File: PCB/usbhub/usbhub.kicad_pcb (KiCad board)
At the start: 2 copper layers, 30.8 x 54.8 mm, 35 parts, among them U1 SL2.1S, U2 SL2.1S

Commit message: case and assembly
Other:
- board size 30.8 x 54.8 mm -> 30.7 x 55 mm
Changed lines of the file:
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@@
 	)
 	(gr_rect
-		(start 148.5 41.75)
+		(start 148.524591 41.518764)
 		(end 179.25 96.5)
+		(radius 2)
 		(stroke
 			(width 0.05)
-			(type default)
+			(type solid)
 		)
 		(fill no)

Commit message: Update usbhub.kicad_pcb
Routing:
- net GND: vias 13 -> 14
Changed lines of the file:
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@@
+	)
+	(via
+		(at 168.22 85.05)
+		(size 0.6)
+		(drill 0.3)
+		(layers "F.Cu" "B.Cu")
+		(net "GND")
 	)
 	(via

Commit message: Update usbhub.kicad_pcb
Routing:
- net /D1B-: track 36.3 -> 36.8 mm
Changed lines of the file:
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@@
+	)
+	(segment
+		(start 170.775 78.594123)
+		(end 170.775 76.075389)
+		(width 0.2)
+		(layer "F.Cu")
+		(net "/D1B-")
+	)
+	(segment
+		(start 169.475 89.55)
+		(end 170.775 88.25)
+		(width 0.2)
+		(layer "F.Cu")
+		(net "/D1B-")
+	)
+	(segment
+		(start 170.324901 84.329337)
+		(end 170.535 84.329337)
+		(width 0.2)
+		(layer "F.Cu")
+		(net "/D1B-")
+	)
+	(segment
+		(start 170.535 81.329337)
+		(end 170.124889 81.329337)
+		(width 0.2)
+		(layer "F.Cu")
+		(net "/D1B-")
+	)
+	(segment
+		(start 170.775 72.593198)
+		(end 169.541782 71.35998)
+		(width 0.2)
+		(layer "F.Cu")
+		(net "/D1B-")
+	)
+	(segment
+		(start 170.775 80.489337)
+		(end 170.775 79.794123)
+		(width 0.2)
+		(layer "F.Cu")
+		(net "/D1B-")
+	)
+	(segment
+		(start 170.324901 86.729337)
+		(end 170.535 86.729337)
+		(width 0.2)
+		(layer "F.Cu")
+		(net "/D1B-")
+	)
+	(segment
+		(start 170.535 84.929337)
+		(end 170.324901 84.929337)
+		(width 0.2)
+		(layer "F.Cu")
+		(net "/D1B-")
+	)
+	(segment
+		(start 169.884889 81.089337)
+		(end 169.884889 80.969337)
+		(width 0.2)
+		(layer "F.Cu")
+		(net "/D1B-")
+	)
+	(segment
+		(start 169.884913 83.489337)
+		(end 169.884913 83.369337)
+		(width 0.2)
+		(layer "F.Cu")
+		(net "/D1B-")
+	)
+	(segment
+		(start 170.124889 80.729337)
+		(end 170.535 80.729337)
+		(width 0.2)
+		(layer "F.Cu")
+		(net "/D1B-")
+	)
+	(segment
+		(start 169.884913 82.289337)
+		(end 169.884913 82.169337)
+		(width 0.2)
+		(layer "F.Cu")
+		(net "/D1B-")
+	)
+	(segment
+		(start 170.324901 85.529337)
+		(end 170.535 85.529337)
+		(width 0.2)
+		(layer "F.Cu")
+		(net "/D1B-")
+	)
+	(segment
+		(start 170.535 86.129337)
+		(end 170.324901 86.129337)
+		(width 0.2)
+		(layer "F.Cu")
+		(net "/D1B-")
 	)
 	(segment
@@
 	)
 	(segment
-		(start 169.475 89.55)
-		(end 170.775 88.25)
-		(width 0.2)
-		(layer "F.Cu")
-		(net "/D1B-")
-	)
-	(segment
-		(start 170.324901 84.329337)
-		(end 170.535 84.329337)
-		(width 0.2)
-		(layer "F.Cu")
-		(net "/D1B-")
-	)
-	(segment
-		(start 170.535 81.329337)
-		(end 170.124889 81.329337)
-		(width 0.2)
-		(layer "F.Cu")
-		(net "/D1B-")
-	)
-	(segment
-		(start 170.324901 86.729337)
-		(end 170.535 86.729337)
-		(width 0.2)
-		(layer "F.Cu")
-		(net "/D1B-")
-	)
-	(segment
-		(start 170.535 84.929337)
-		(end 170.324901 84.929337)
-		(width 0.2)
-		(layer "F.Cu")
-		(net "/D1B-")
-	)
-	(segment
-		(start 169.884889 81.089337)
-		(end 169.884889 80.969337)
-		(width 0.2)
-		(layer "F.Cu")
-		(net "/D1B-")
-	)
-	(segment
-		(start 169.884913 83.489337)
-		(end 169.884913 83.369337)
-		(width 0.2)
-		(layer "F.Cu")
-		(net "/D1B-")
-	)
-	(segment
-		(start 170.775 72.593198)
-		(end 169.541782 71.35998)
-		(width 0.2)
-		(layer "F.Cu")
-		(net "/D1B-")
-	)
-	(segment
-		(start 170.124889 80.729337)
-		(end 170.535 80.729337)
-		(width 0.2)
-		(layer "F.Cu")
-		(net "/D1B-")
-	)
-	(segment
-		(start 169.884913 82.289337)
-		(end 169.884913 82.169337)
-		(width 0.2)
-		(layer "F.Cu")
-		(net "/D1B-")
-	)
-	(segment
-		(start 170.324901 85.529337)
-		(end 170.535 85.529337)
-		(width 0.2)
-		(layer "F.Cu")
-		(net "/D1B-")
-	)
-	(segment
-		(start 170.535 86.129337)
-		(end 170.324901 86.129337)
+		(start 170.084901 84.689337)
+		(end 170.084901 84.569337)
+		(width 0.2)
+		(layer "F.Cu")
+		(net "/D1B-")
+	)
+	(segment
+		(start 170.775 81.689337)
+		(end 170.775 81.569337)
+		(width 0.2)
+		(layer "F.Cu")
+		(net "/D1B-")
+	)
+	(segment
+		(start 161.39002 68.842073)
+		(end 161.39002 67.89002)
+		(width 0.2)
+		(layer "F.Cu")
+		(net "/D1B-")
+	)
+	(segment
+		(start 170.124913 81.929337)
+		(end 170.535 81.929337)
+		(width 0.2)
+		(layer "F.Cu")
+		(net "/D1B-")
+	)
+	(segment
+		(start 170.775 88.25)
+		(end 170.775 87.569337)
+		(width 0.2)
+		(layer "F.Cu")
+		(net "/D1B-")
+	)
+	(segment
+		(start 170.535 82.529337)
+		(end 170.124913 82.529337)
+		(width 0.2)
+		(layer "F.Cu")
+		(net "/D1B-")
+	)
+	(segment
+		(start 170.084901 87.089337)
+		(end 170.084901 86.969337)
+		(width 0.2)
+		(layer "F.Cu")
+		(net "/D1B-")
+	)
+	(segment
+		(start 170.535 83.729337)
+		(end 170.124913 83.729337)
+		(width 0.2)
+		(layer "F.Cu")
+		(net "/D1B-")
+	)
+	(segment
+		(start 170.775 82.889337)
+		(end 170.775 82.769337)
+		(width 0.2)
+		(layer "F.Cu")
+		(net "/D1B-")
+	)
+	(segment
+		(start 170.775 78.721951)
+		(end 170.775 78.594123)
+		(width 0.2)
+		(layer "F.Cu")
+		(net "/D1B-")
+	)
+	(segment
+		(start 170.302828 79.321951)
+		(end 170.302828 79.194123)
+		(width 0.2)
+		(layer "F.Cu")
+		(net "/D1B-")
+	)
+	(segment
+		(start 170.775 85.289337)
+		(end 170.775 85.169337)
+		(width 0.2)
+		(layer "F.Cu")
+		(net "/D1B-")
+	)
+	(segment
+		(start 170.535 87.329337)
+		(end 170.324901 87.329337)
 		(width 0.2)
 		(layer "F.Cu")
@@
 	)
 	(segment
+		(start 170.775 76.075389)
+		(end 170.775 72.593198)
+		(width 0.2)
+		(layer "F.Cu")
+		(net "/D1B-")
+	)
+	(segment
 		(start 169.541782 71.35998)
 		(end 163.907927 71.35998)
-		(width 0.2)
-		(layer "F.Cu")
-		(net "/D1B-")
-	)
-	(segment
-		(start 170.084901 84.689337)
-		(end 170.084901 84.569337)
-		(width 0.2)
-		(layer "F.Cu")
-		(net "/D1B-")
-	)
-	(segment
-		(start 170.775 81.689337)
-		(end 170.775 81.569337)
-		(width 0.2)
-		(layer "F.Cu")
-		(net "/D1B-")
-	)
-	(segment
-		(start 170.124913 81.929337)
-		(end 170.535 81.929337)
-		(width 0.2)
-		(layer "F.Cu")
-		(net "/D1B-")
-	)
-	(segment
-		(start 170.775 88.25)
-		(end 170.775 87.569337)
-		(width 0.2)
-		(layer "F.Cu")
-		(net "/D1B-")
-	)
-	(segment
-		(start 170.535 82.529337)
-		(end 170.124913 82.529337)
-		(width 0.2)
-		(layer "F.Cu")
-		(net "/D1B-")
-	)
-	(segment
-		(start 170.084901 87.089337)
-		(end 170.084901 86.969337)
-		(width 0.2)
-		(layer "F.Cu")
-		(net "/D1B-")
-	)
-	(segment
-		(start 170.535 83.729337)
-		(end 170.124913 83.729337)
-		(width 0.2)
-		(layer "F.Cu")
-		(net "/D1B-")
-	)
-	(segment
-		(start 170.775 82.889337)
-		(end 170.775 82.769337)
-		(width 0.2)
-		(layer "F.Cu")
-		(net "/D1B-")
-	)
-	(segment
-		(start 161.39002 68.842073)
-		(end 161.39002 67.89002)
-		(width 0.2)
-		(layer "F.Cu")
-		(net "/D1B-")
-	)
-	(segment
-		(start 170.775 80.489337)
-		(end 170.775 72.593198)
-		(width 0.2)
-		(layer "F.Cu")
-		(net "/D1B-")
-	)
-	(segment
-		(start 170.775 85.289337)
-		(end 170.775 85.169337)
-		(width 0.2)
-		(layer "F.Cu")
-		(net "/D1B-")
-	)
-	(segment
-		(start 170.535 87.329337)
-		(end 170.324901 87.329337)
 		(width 0.2)
 		(layer "F.Cu")
@@
 	)
 	(arc
+		(start 170.302828 79.194123)
+		(mid 170.371976 79.027185)
+		(end 170.538914 78.958037)
+		(width 0.2)
+		(layer "F.Cu")
+		(net "/D1B-")
+	)
+	(arc
 		(start 170.775 82.769337)
 		(mid 170.704706 82.599631)
@@
 	)
 	(arc
+		(start 170.538914 78.958037)
+		(mid 170.705852 78.888889)
+		(end 170.775 78.721951)
+		(width 0.2)
+		(layer "F.Cu")
+		(net "/D1B-")
+	)
+	(arc
 		(start 169.884913 83.369337)
 		(mid 169.955207 83.199631)
@@
 	)
 	(arc
+		(start 170.775 79.794123)
+		(mid 170.705852 79.627185)
+		(end 170.538914 79.558037)
+		(width 0.2)
+		(layer "F.Cu")
+		(net "/D1B-")
+	)
+	(arc
 		(start 170.124889 81.329337)
 		(mid 169.955183 81.259043)
@@
 		(mid 170.704706 81.399631)
 		(end 170.535 81.329337)
+		(width 0.2)
+		(layer "F.Cu")
+		(net "/D1B-")
+	)
+	(arc
+		(start 170.538914 79.558037)
+		(mid 170.371976 79.488889)
+		(end 170.302828 79.321951)
 		(width 0.2)
 		(layer "F.Cu")
@@
 	)
 	(generated
+		(type tuning_pattern)
+		(name "Tuning Pattern")
+		(layer "F.Cu")
+		(base_line
+			(pts
+				(xy 170.775 79.794123) (xy 170.775 76.075389)
+			)
+		)
+		(base_line_coupled
+			(pts
+				(xy 171.225 79.794123) (xy 171.225 79.810099)
+			)
+		)
+		(corner_radius_percent 80)
+		(end
+			(xy 170.775 76.075389)
+		)
+		(initial_side "left")
+		(is_time_domain no)
+		(last_diff_pair_gap 0.18)
+		(last_netname "/D1B-")
+		(last_status "tuned")
+		(last_track_width 0.2)
+		(last_tuning_length -5.6e-05)
+		(max_amplitude 1)
+		(min_amplitude 0.2)
+		(min_spacing 0.6)
+		(origin
+			(xy 170.775 79.794123)
+		)
+		(override_custom_rules no)
+		(rounded yes)
+		(single_sided no)
+		(target_delay 1000000)
+		(target_delay_max 1000000)
+		(target_delay_min 0)
+		(target_length 1000000)
+		(target_length_max 1000000)
+		(target_length_min 0)
+		(target_skew 0)
+		(target_skew_max 0.1)
+		(target_skew_min -0.1)
+		(tuning_mode "diff_pair_skew")
+		(members "1dece349-dbe6-4893-8c04-211b6d402d7a" "26bfc59c-0bca-4a53-af13-9448fa790285"
+			"31407be5-377e-49e6-b739-af8d52b4daab" "53a43092-9930-406d-b0c2-06b6def7a89c"
+			"75226c4a-ea9a-4ce0-b9c3-285e020652f5" "aa32028f-71d7-4b5e-87e4-8afc0a5836df"
+			"aab755b0-ae1c-4e58-aaa0-9a94909e4790"
+		)
+	)
+	(generated

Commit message: update all the steps
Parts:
- added H1: MountingHole, MountingHole:MountingHole_3.2mm_M3, F.Cu at (152.5, 45.5)
- added H2: MountingHole, MountingHole:MountingHole_3.2mm_M3, F.Cu at (163.5, 93.0)
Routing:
- net /VBUS: track 187.3 -> 185.5 mm
- net /D4B-: track 21.0 -> 22.6 mm
- net /D4B+: track 22.5 -> 23.8 mm

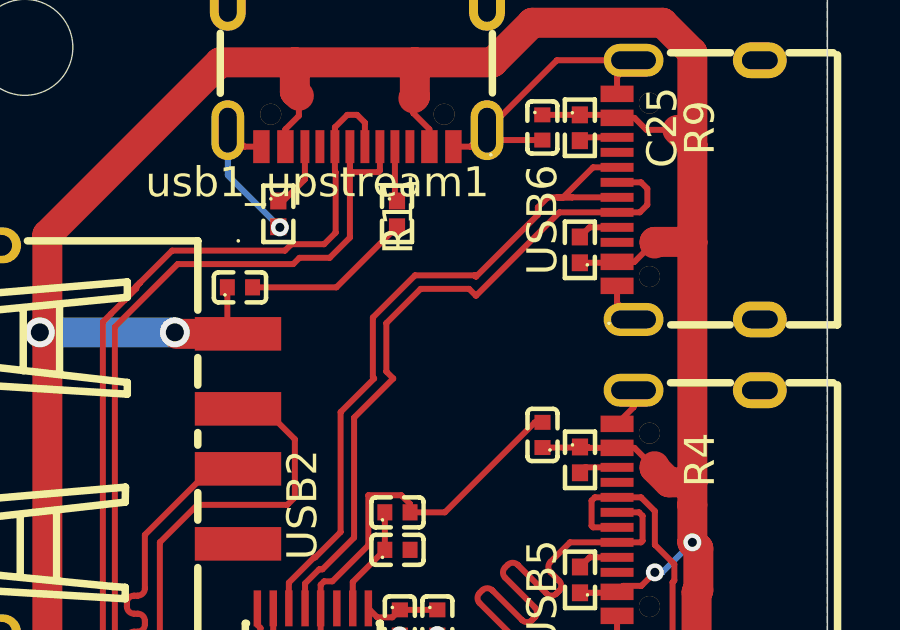
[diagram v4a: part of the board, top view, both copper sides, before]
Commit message: no curvy trace around nonexistent hole
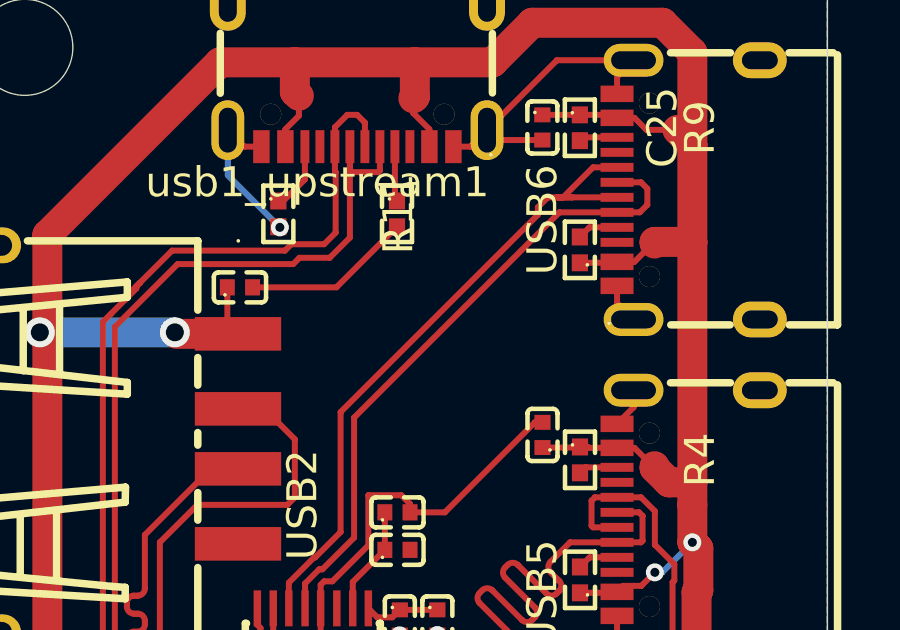
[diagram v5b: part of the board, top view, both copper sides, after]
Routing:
- net /D4B-: track 22.6 -> 21.0 mm
- net /D4B+: track 23.8 -> 22.5 mm
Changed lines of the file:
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@@
 	)
 	(segment
-		(start 171.44 49.5)
-		(end 170.44 50.5)
+		(start 169.934314 50.5)
+		(end 170.75 50.5)
 		(width 0.2)
 		(layer "F.Cu")
@@
 	)
 	(segment
+		(start 171.44 49.5)
+		(end 170.44 50.5)
+		(width 0.2)
+		(layer "F.Cu")
+		(net "/D4B+")
+	)
+	(segment
 		(start 172.24 50.5)
 		(end 170.75 50.5)
+		(width 0.2)
+		(layer "F.Cu")
+		(net "/D4B+")
+	)
+	(segment
+		(start 161.3 63.34363)
+		(end 162.14363 62.5)
+		(width 0.2)
+		(layer "F.Cu")
+		(net "/D4B+")
+	)
+	(segment
+		(start 170.44 50.5)
+		(end 170.25 50.5)
+		(width 0.2)
+		(layer "F.Cu")
+		(net "/D4B+")
+	)
+	(segment
+		(start 163.025 57.656802)
+		(end 169.6 51.081802)
+		(width 0.2)
+		(layer "F.Cu")
+		(net "/D4B+")
+	)
+	(segment
+		(start 169.6 51.081802)
+		(end 169.6 50.834314)
+		(width 0.2)
+		(layer "F.Cu")
+		(net "/D4B+")
+	)
+	(segment
+		(start 162.181802 62.5)
+		(end 163.025 61.656802)
+		(width 0.2)
+		(layer "F.Cu")
+		(net "/D4B+")
+	)
+	(segment
+		(start 172.24 49.5)
+		(end 171.44 49.5)
+		(width 0.2)
+		(layer "F.Cu")
+		(net "/D4B+")
+	)
+	(segment
+		(start 170.25 50.5)
+		(end 170.75 50.5)
+		(width 0.2)
+		(layer "F.Cu")
+		(net "/D4B+")
+	)
+	(segment
+		(start 163.025 61.656802)
+		(end 163.025 57.656802)
+		(width 0.2)
+		(layer "F.Cu")
+		(net "/D4B+")
+	)
+	(segment
+		(start 169.6 50.834314)
+		(end 169.934314 50.5)
 		(width 0.2)
 		(layer "F.Cu")
@@
 	)
 	(segment
-		(start 169.934314 50.5)
-		(end 170.75 50.5)
+		(start 161.84 63.725)
+		(end 161.84 63.369315)
 		(width 0.2)
 		(layer "F.Cu")
-		(net "/D4B+")
+		(net "/D4B-")
 	)
 	(segment
-		(start 162.181802 62.5)
-		(end 163.025 61.656802)
-		(width 0.2)
-		(layer "F.Cu")
-		(net "/D4B+")
-	)
-	(segment
-		(start 170.44 50.5)
-		(end 170.25 50.5)
-		(width 0.2)
-		(layer "F.Cu")
-		(net "/D4B+")
-	)
-	(segment
-		(start 164.10002 54.505896)
-		(end 165.505896 53.10002)
-		(width 0.2)
-		(layer "F.Cu")
-		(net "/D4B+")
-	)
-	(segment
-		(start 164.10002 56.494104)
-		(end 164.10002 54.505896)
-		(width 0.2)
-		(layer "F.Cu")
-		(net "/D4B+")
-	)
-	(segment
-		(start 167.494104 53.10002)
-		(end 167.537943 53.143859)
-		(width 0.2)
-		(layer "F.Cu")
-		(net "/D4B+")
-	)
-	(segment
-		(start 172.24 49.5)
-		(end 171.44 49.5)
-		(width 0.2)
-		(layer "F.Cu")
-		(net "/D4B+")
-	)
-	(segment
-		(start 167.537943 53.143859)
-		(end 169.6 51.081802)
-		(width 0.2)
-		(layer "F.Cu")
-		(net "/D4B+")
-	)
-	(segment
-		(start 170.25 50.5)
-		(end 170.75 50.5)
-		(width 0.2)
-		(layer "F.Cu")
-		(net "/D4B+")
-	)
-	(segment
-		(start 164.143859 56.537943)
-		(end 164.10002 56.494104)
-		(width 0.2)
-		(layer "F.Cu")
-		(net "/D4B+")
-	)
-	(segment
-		(start 169.6 50.834314)
-		(end 169.934314 50.5)
-		(width 0.2)
-		(layer "F.Cu")
-		(net "/D4B+")
-	)
-	(segment
-		(start 161.3 63.34363)
-		(end 162.14363 62.5)
-		(width 0.2)
-		(layer "F.Cu")
-		(net "/D4B+")
-	)
-	(segment
-		(start 163.025 57.656802)
-		(end 164.143859 56.537943)
-		(width 0.2)
-		(layer "F.Cu")
-		(net "/D4B+")
-	)
-	(segment
-		(start 163.025 61.656802)
-		(end 163.025 57.656802)
-		(width 0.2)
-		(layer "F.Cu")
-		(net "/D4B+")
-	)
-	(segment
-		(start 165.505896 53.10002)
-		(end 167.494104 53.10002)
-		(width 0.2)
-		(layer "F.Cu")
-		(net "/D4B+")
-	)
-	(segment
-		(start 169.6 51.081802)
-		(end 169.6 50.834314)
-		(width 0.2)
-		(layer "F.Cu")
-		(net "/D4B+")
-	)
-	(segment
-		(start 164.780241 56.537957)
-		(end 164.55 56.307716)
+		(start 163.475 57.843198)
+		(end 170.318198 51)
 		(width 0.2)
 		(layer "F.Cu")
@@
 	)
 	(segment
-		(start 162.309315 62.9)
-		(end 162.418198 62.9)
-		(width 0.2)
-		(layer "F.Cu")
-		(net "/D4B-")
-	)
-	(segment
 		(start 173 51)
 		(end 172.24 51)
-		(width 0.2)
-		(layer "F.Cu")
-		(net "/D4B-")
-	)
-	(segment
-		(start 164.55 54.692284)
-		(end 165.692284 53.55)
 		(width 0.2)
 		(layer "F.Cu")
@@
 	)
 	(segment
-		(start 167.537957 53.780241)
-		(end 170.318198 51)
+		(start 173.25 50.75)
+		(end 173 51)
+		(width 0.2)
+		(layer "F.Cu")
+		(net "/D4B-")
+	)
+	(segment
+		(start 173.25 50.21)
+		(end 173.25 50.75)
+		(width 0.2)
+		(layer "F.Cu")
+		(net "/D4B-")
+	)
+	(segment
+		(start 162.309315 62.9)
+		(end 162.418198 62.9)
 		(width 0.2)
 		(layer "F.Cu")
@@
 	)
 	(segment
-		(start 173.25 50.75)
-		(end 173 51)
-		(width 0.2)
-		(layer "F.Cu")
-		(net "/D4B-")
-	)
-	(segment
-		(start 163.475 57.843198)
-		(end 164.780241 56.537957)
-		(width 0.2)
-		(layer "F.Cu")
-		(net "/D4B-")
-	)
-	(segment
-		(start 173.25 50.21)
-		(end 173.25 50.75)
-		(width 0.2)
-		(layer "F.Cu")
-		(net "/D4B-")
-	)
-	(segment
 		(start 163.475 61.843198)
 		(end 163.475 57.843198)
 		(width 0.2)
 		(layer "F.Cu")
-		(net "/D4B-")
-	)
-	(segment
-		(start 165.692284 53.55)
-		(end 167.307716 53.55)
-		(width 0.2)
-		(layer "F.Cu")
-		(net "/D4B-")
-	)
-	(segment
-		(start 161.84 63.725)
-		(end 161.84 63.369315)
-		(width 0.2)
-		(layer "F.Cu")
-		(net "/D4B-")
-	)
-	(segment
-		(start 164.55 56.307716)
-		(end 164.55 54.692284)
-		(width 0.2)
-		(layer "F.Cu")
-		(net "/D4B-")
-	)
-	(segment
-		(start 167.307716 53.55)
-		(end 167.537957 53.780241)
-		(width 0.2)
-		(layer "F.Cu")
